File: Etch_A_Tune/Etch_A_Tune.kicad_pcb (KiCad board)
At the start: 4 copper layers, 114.5 x 99.7 mm, 108 parts, among them J1 75915-414LF, J2 91601-304ALF, J4 2171790001, J5 SJ-3524-SMT-PI, J7 3220-10-0300-00, U1 BQ297xy, U2 CSD16406Q3, U3 CSD16406Q3, U4 TPS62063DSGR, U5 STM32H7A3ZIT6Q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

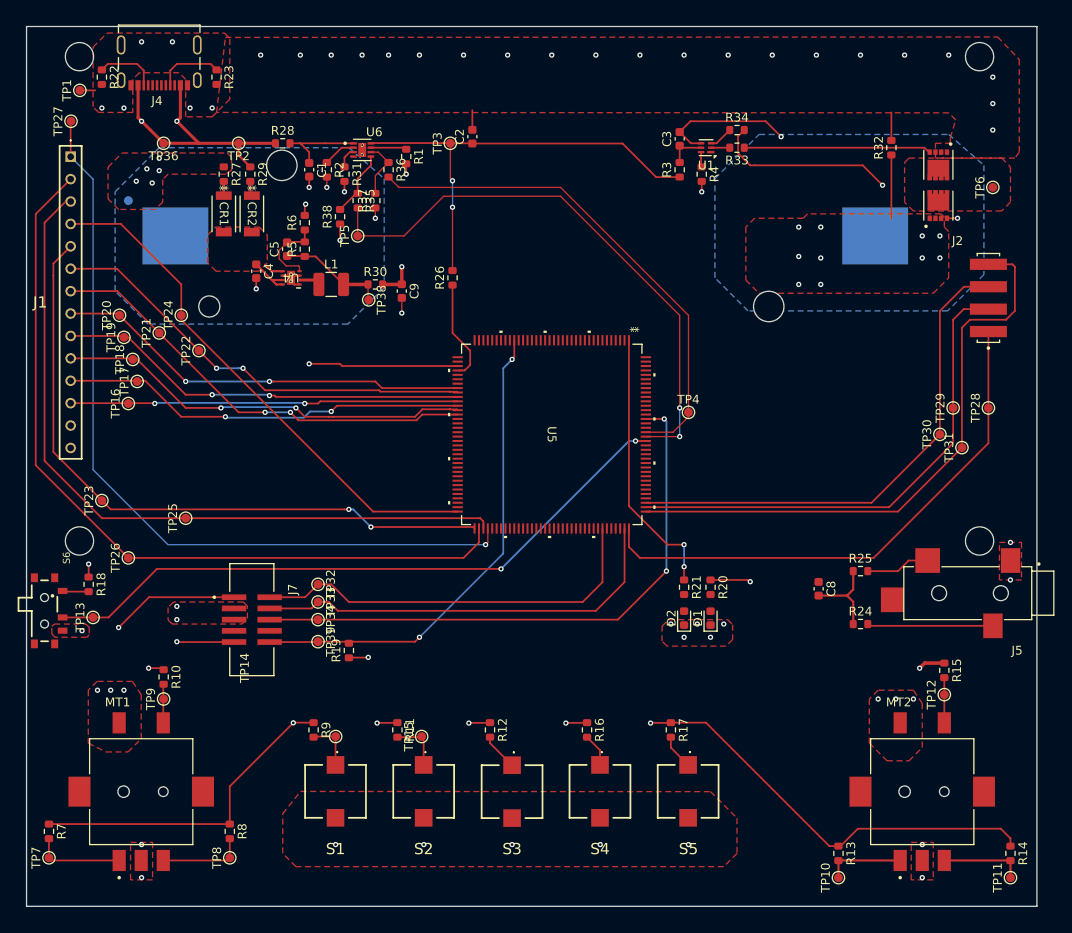
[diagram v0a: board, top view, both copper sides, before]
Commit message: 2 Layer Board
Changed from 4 to 2 layers
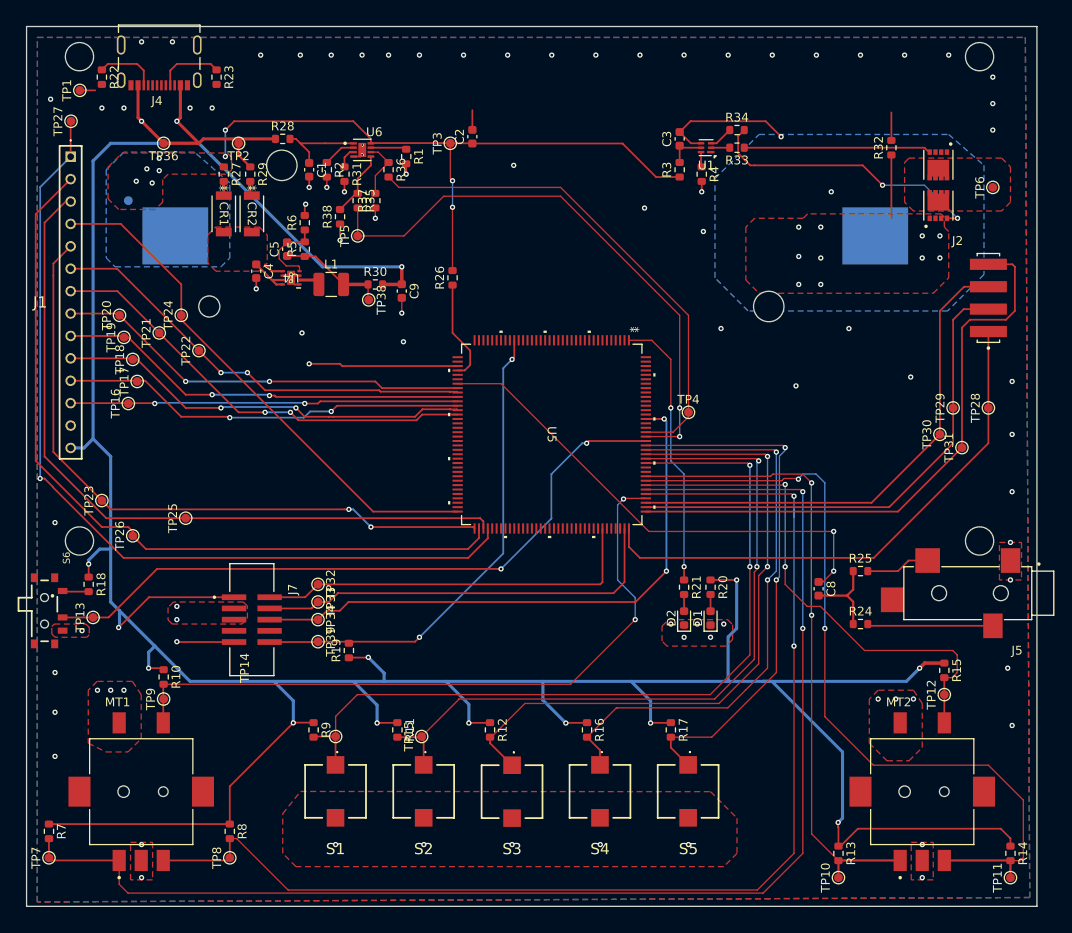
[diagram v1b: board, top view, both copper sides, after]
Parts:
- moved TP26 2.55 mm to (29.0, 77.7)
- moved R28 0.50 mm to (46.0, 32.7)
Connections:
- U6 pad 11: (no net) -> GND
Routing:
- net /Controllers/ROTA1: track 10.3 -> 151.6 mm, vias 0 -> 2
- net /Controllers/ROTB1: track 9.84 -> 137.0 mm, vias 0 -> 2
- net /Controllers/SW1: track 5.75 -> 91.3 mm, vias 0 -> 2
- net /Controllers/ROTB2: track 9.44 -> 91.6 mm, vias 0 -> 2
- net /Controllers/SW2: track 6.09 -> 83.1 mm, vias 0 -> 2
- net /Controllers/ROTP1: track 4.39 -> 78.2 mm, vias 0 -> 2
- net /Controllers/SW3: track 4.21 -> 75.9 mm, vias 0 -> 2
- net /Controllers/SW4: track 3.75 -> 67.3 mm, vias 0 -> 2
- net /Controllers/ROTA2: track 8.94 -> 72.4 mm, vias 0 -> 2
- net /Controllers/SW5: track 3.95 -> 60.8 mm, vias 0 -> 2
- net /Microcontroller/DAC_OUT: track 0.00 -> 56.3 mm, vias 0 -> 2
- net /Controllers/ROTP2: track 5.12 -> 58.8 mm, vias 0 -> 2
- net +3.3V: track 343.3 -> 365.2 mm, vias 12 -> 13
- net /Battery/PACK+: track 51.1 -> 72.4 mm, vias 7 -> 9
- net /T_IRQ: track 90.5 -> 98.5 mm
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- added copper zone on B.Cu, net GND
- removed copper zone on In1.Cu, net GND
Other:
- copper layers 4 -> 2

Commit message: Update
Finished Analog Power Domain
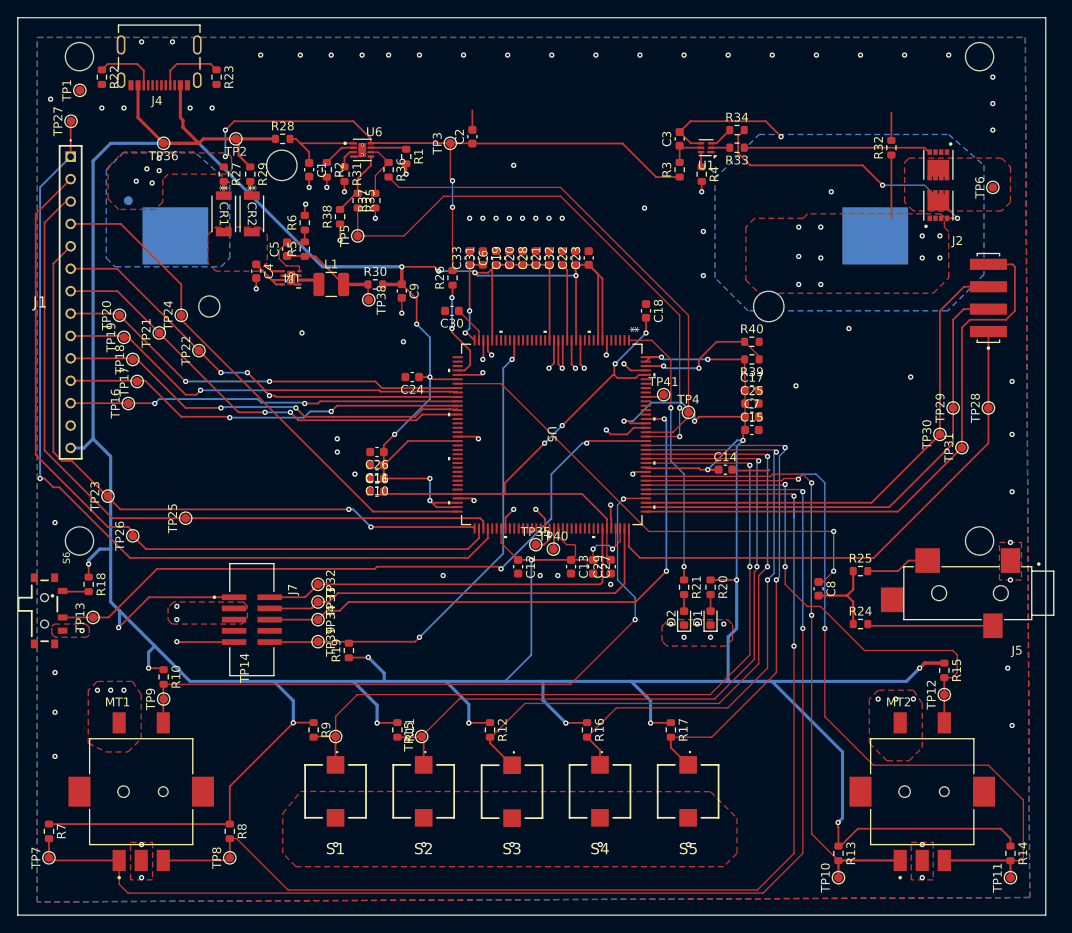
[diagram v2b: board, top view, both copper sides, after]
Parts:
- added C10: 100nF, Capacitor_SMD:C_0603_1608Metric, F.Cu at (56.7, 71.2)
- added C11: 100nF, Capacitor_SMD:C_0603_1608Metric, F.Cu at (56.7, 69.7)
- added C12: 1uF, Capacitor_SMD:C_0603_1608Metric, F.Cu at (72.7, 81.2)
- added C13: 100nF, Capacitor_SMD:C_0603_1608Metric, F.Cu at (78.7, 81.2)
- added C14: 100nF, Capacitor_SMD:C_0603_1608Metric, F.Cu at (96.2, 70.2)
- added C15: 100nF, Capacitor_SMD:C_0603_1608Metric, F.Cu at (99.2, 65.7)
- added C16: 100nF, Capacitor_SMD:C_0603_1608Metric, F.Cu at (56.7, 72.7)
- added C17: 100nF, Capacitor_SMD:C_0603_1608Metric, F.Cu at (99.2, 61.2)
- added C18: 100nF, Capacitor_SMD:C_0603_1608Metric, F.Cu at (87.2, 52.2)
- added C19: 100nF, Capacitor_SMD:C_0603_1608Metric, F.Cu at (71.7, 46.2)
- added C20: 100nF, Capacitor_SMD:C_0603_1608Metric, F.Cu at (73.2, 46.2)
- added C21: 100nF, Capacitor_SMD:C_0603_1608Metric, F.Cu at (76.2, 46.2)
- added C22: 100nF, Capacitor_SMD:C_0603_1608Metric, F.Cu at (79.2, 46.2)
- added C23: 100nF, Capacitor_SMD:C_0603_1608Metric, F.Cu at (80.7, 46.2)
- added C24: 100nF, Capacitor_SMD:C_0603_1608Metric, F.Cu at (60.7, 59.7)
- added C25: 1uF, Capacitor_SMD:C_0603_1608Metric, F.Cu at (99.2, 62.7)
- added C26: 100nF, Capacitor_SMD:C_0603_1608Metric, F.Cu at (56.7, 68.2)
- added C27: 4.7uF, Capacitor_SMD:C_0603_1608Metric, F.Cu at (81.2, 81.2)
- added C28: 100nF, Capacitor_SMD:C_0603_1608Metric, F.Cu at (74.7, 46.2)
- added C29: 100nF, Capacitor_SMD:C_0603_1608Metric, F.Cu at (83.2, 81.2)
- added C30: 1uF, Capacitor_SMD:C_0603_1608Metric, F.Cu at (65.2, 52.2)
- added C31: 1uF, Capacitor_SMD:C_0603_1608Metric, F.Cu at (68.7, 46.2)
- added C32: 220pF, Capacitor_SMD:C_0603_1608Metric, F.Cu at (77.7, 46.2)
- added C33: 1nF, Capacitor_SMD:C_0603_1608Metric, F.Cu at (67.2, 46.2)
- added C6: 100nF, Capacitor_SMD:C_0603_1608Metric, F.Cu at (70.2, 46.2)
- added C7: 100nF, Capacitor_SMD:C_0603_1608Metric, F.Cu at (99.2, 64.2)
- added R39: 0, Resistor_SMD:R_0603_1608Metric, F.Cu at (99.2, 57.7)
- added R40: 0, Resistor_SMD:R_0603_1608Metric, F.Cu at (99.2, 55.7)
- added TP35: USB5V, TestPoint:TestPoint_Pad_D1.0mm, F.Cu at (74.7, 78.7)
- added TP40: USB3V3, TestPoint:TestPoint_Pad_D1.0mm, F.Cu at (76.7, 79.2)
- added TP41: BOOT0, TestPoint:TestPoint_Pad_D1.0mm, F.Cu at (89.2, 61.7)
- moved TP23 0.85 mm to (26.2, 73.2)
- moved TP2 0.59 mm to (40.7, 32.7)
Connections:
- U5 pad 103: unconnected-(U5B-VCAP-Pad103) -> VCORE
- U5 pad 104: unconnected-(U5B-VSS-Pad104) -> GND
- U5 pad 105: unconnected-(U5B-VDDLDO-Pad105) -> +3.3V
- U5 pad 106: unconnected-(U5B-VDD-Pad106) -> +3.3V
- U5 pad 118: unconnected-(U5B-VSS-Pad118) -> GND
- U5 pad 119: unconnected-(U5B-VDDMMC-Pad119) -> +3.3V
- U5 pad 12: unconnected-(U5A-VSS-Pad12) -> GND
- U5 pad 128: unconnected-(U5B-VSS-Pad128) -> GND
- U5 pad 129: unconnected-(U5B-VDD-Pad129) -> +3.3V
- U5 pad 13: unconnected-(U5A-VDD-Pad13) -> +3.3V
- U5 pad 135: unconnected-(U5B-BOOT0-Pad135) -> Net-(U5B-BOOT0)
- U5 pad 14: unconnected-(U5A-VSSSMPS-Pad14) -> GND
- U5 pad 140: unconnected-(U5B-VCAP-Pad140) -> VCORE
- U5 pad 141: unconnected-(U5B-VSS-Pad141) -> GND
- U5 pad 142: unconnected-(U5B-PDR_ON-Pad142) -> Net-(U5B-PDR_ON)
- U5 pad 143: unconnected-(U5B-VDDLDO-Pad143) -> +3.3V
- U5 pad 144: unconnected-(U5B-VDD-Pad144) -> +3.3V
- U5 pad 15: unconnected-(U5A-VLXSMPS-Pad15) -> Net-(U5A-VLXSMPS)
- U5 pad 16: unconnected-(U5A-VDDSMPS-Pad16) -> GND
- U5 pad 17: unconnected-(U5A-VFBSMPS-Pad17) -> GND
- U5 pad 18: unconnected-(U5A-VSS-Pad18) -> GND
- U5 pad 19: unconnected-(U5A-VDD-Pad19) -> +3.3V
- U5 pad 32: unconnected-(U5A-VDD-Pad32) -> +3.3V
- U5 pad 33: unconnected-(U5A-VSS-Pad33) -> GND
- U5 pad 34: unconnected-(U5A-VSSA-Pad34) -> GND
- U5 pad 35: unconnected-(U5A-VREF+-Pad35) -> Net-(U5A-VREF+)
- U5 pad 36: unconnected-(U5A-VDDA-Pad36) -> Net-(U5A-VDDA)
- U5 pad 37: PA0 -> unconnected-(U5A-PA0-Pad37)
- U5 pad 38: PA1 -> unconnected-(U5A-PA1-Pad38)
- U5 pad 39: PA2 -> unconnected-(U5A-PA2-Pad39)
- U5 pad 41: unconnected-(U5A-VSS-Pad41) -> GND
- U5 pad 42: unconnected-(U5A-VDD-Pad42) -> +3.3V
- U5 pad 55: unconnected-(U5A-VSS-Pad55) -> GND
- U5 pad 56: unconnected-(U5A-VDD-Pad56) -> +3.3V
- U5 pad 6: unconnected-(U5A-VSS-Pad6) -> GND
- U5 pad 68: unconnected-(U5A-VCAP-Pad68) -> VCORE
- U5 pad 69: unconnected-(U5A-VSS-Pad69) -> GND
- U5 pad 7: unconnected-(U5A-VDD-Pad7) -> +3.3V
- U5 pad 70: unconnected-(U5A-VDDLDO-Pad70) -> +3.3V
- U5 pad 71: unconnected-(U5A-VDD-Pad71) -> +3.3V
- U5 pad 79: unconnected-(U5B-VDD-Pad79) -> +3.3V
- U5 pad 8: unconnected-(U5A-VBAT-Pad8) -> +3.3V
- U5 pad 80: unconnected-(U5B-VSS-Pad80) -> GND
- U5 pad 89: unconnected-(U5B-VSS-Pad89) -> GND
- U5 pad 9: PC13 -> unconnected-(U5A-PC13-Pad9)
- U5 pad 90: unconnected-(U5B-VDD50USB-Pad90) -> Net-(U5B-VDD50USB)
- U5 pad 91: unconnected-(U5B-VDD33USB-Pad91) -> Net-(U5B-VDD33USB)
- U5 pad 92: unconnected-(U5B-VDD-Pad92) -> +3.3V
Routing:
- net +3.3V: track 365.2 -> 607.7 mm, vias 13 -> 30
- net VCORE: track 0.00 -> 62.0 mm, vias 0 -> 4
- net GND: track 30.1 -> 79.6 mm, vias 83 -> 114
- net PA2: track 16.9 -> 0.00 mm, vias 1 -> 0
- net Net-(U5B-PDR_ON): track 0.00 -> 15.8 mm, vias 0 -> 2
- net Net-(U5A-VDDA): track 0.00 -> 10.8 mm, vias 0 -> 2
- net Net-(U5A-VLXSMPS): track 0.00 -> 8.79 mm
- net Net-(U5A-VREF+): track 0.00 -> 4.28 mm
- net Net-(U5B-VDD50USB): track 0.00 -> 3.03 mm
- net Net-(U5B-VDD33USB): track 0.00 -> 2.36 mm
- net Net-(U5B-BOOT0): track 0.00 -> 2.12 mm
- net /Battery/USB_Charge: track 31.7 -> 32.0 mm, vias 2 -> 0
- net /Battery/BAT_V_SENSE: vias 0 -> 2
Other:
- board size 114.5 x 99.7 mm -> 116.5 x 101.7 mm

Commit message: 95% finished PCB
Only changes needed for completion is ferrite bead footprint and DNP crystal osc.
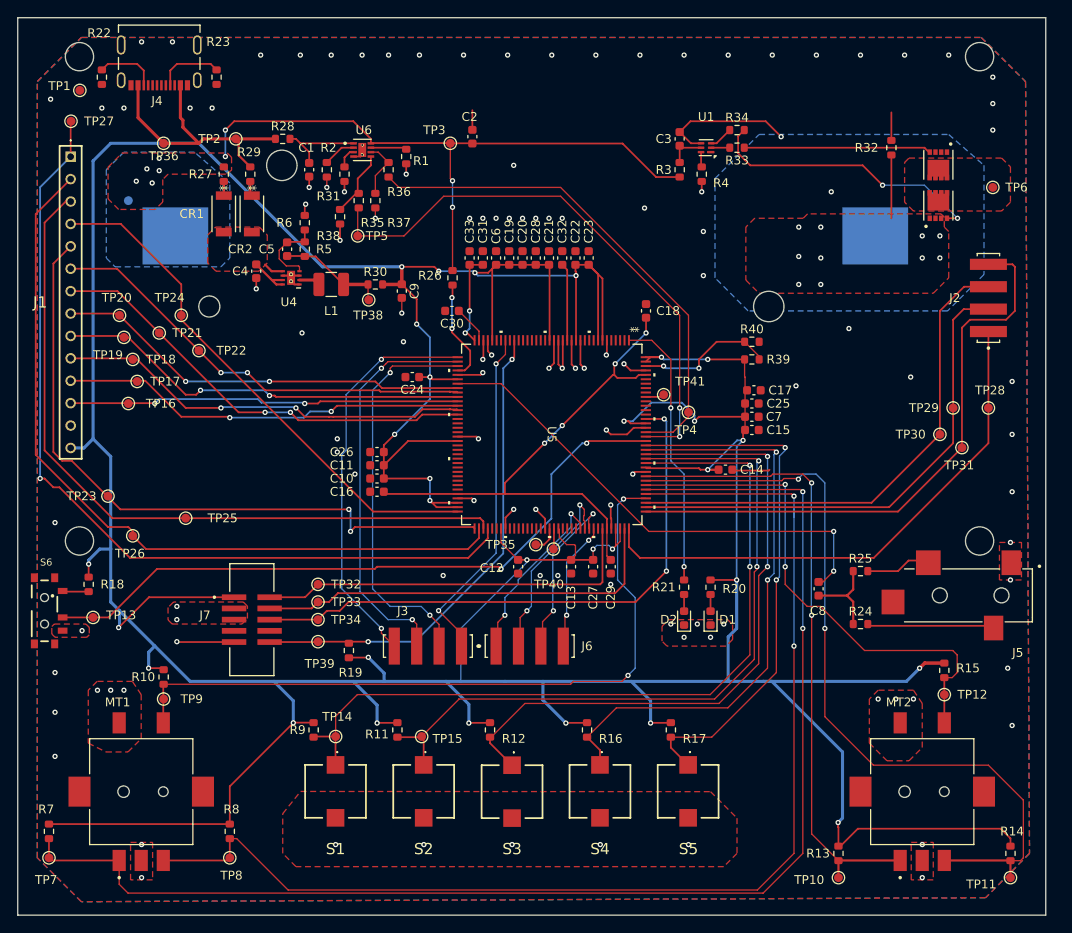
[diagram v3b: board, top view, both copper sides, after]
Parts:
- added J3: 91601-304ALF, BQ25170DSGR:AMPHENOL_91601-304ALF, F.Cu at (62.5, 90.2)
- added J6: 91601-304ALF, BQ25170DSGR:AMPHENOL_91601-304ALF, F.Cu at (74.0, 90.2)
- moved J5 0.26 mm to (127.5, 84.5)
- moved C17 0.22 mm to (99.5, 61.2)
- moved R35 0.12 mm to (54.7, 39.7)
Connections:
- U4 pad V: GND -> (no net)
- U5 pad 100: unconnected-(U5B-PA11-Pad100) -> /PA11
- U5 pad 29: unconnected-(U5A-PC1-Pad29) -> /PC1
- U5 pad 37: unconnected-(U5A-PA0-Pad37) -> /PA0
- U5 pad 38: unconnected-(U5A-PA1-Pad38) -> /PA1
- U5 pad 39: unconnected-(U5A-PA2-Pad39) -> /PA2
- U5 pad 97: unconnected-(U5B-PA8-Pad97) -> /PA8
- U5 pad 98: unconnected-(U5B-PA9-Pad98) -> /PA9
- U5 pad 99: unconnected-(U5B-PA10-Pad99) -> /PA10
- U6 pad 10: GND -> (no net)
- U6 pad 11: GND -> (no net)
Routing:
- net /PA1: track 0.00 -> 45.8 mm, vias 0 -> 2
- net /PA0: track 0.00 -> 45.6 mm, vias 0 -> 2
- net /PA2: track 0.00 -> 45.3 mm, vias 0 -> 2
- net /PC1: track 0.00 -> 38.9 mm, vias 0 -> 2
- net /PA9: track 0.00 -> 21.8 mm, vias 0 -> 2
- net /PA8: track 0.00 -> 20.6 mm, vias 0 -> 2
- net /PA10: track 0.00 -> 19.3 mm, vias 0 -> 2
- net /PA11: track 0.00 -> 14.7 mm, vias 0 -> 2
- net /Controllers/ROTP1: track 78.2 -> 81.5 mm
- net +3.3V: track 607.7 -> 609.6 mm
- net /T_CLK: track 75.5 -> 77.2 mm
